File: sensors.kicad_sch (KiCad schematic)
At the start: 10 parts

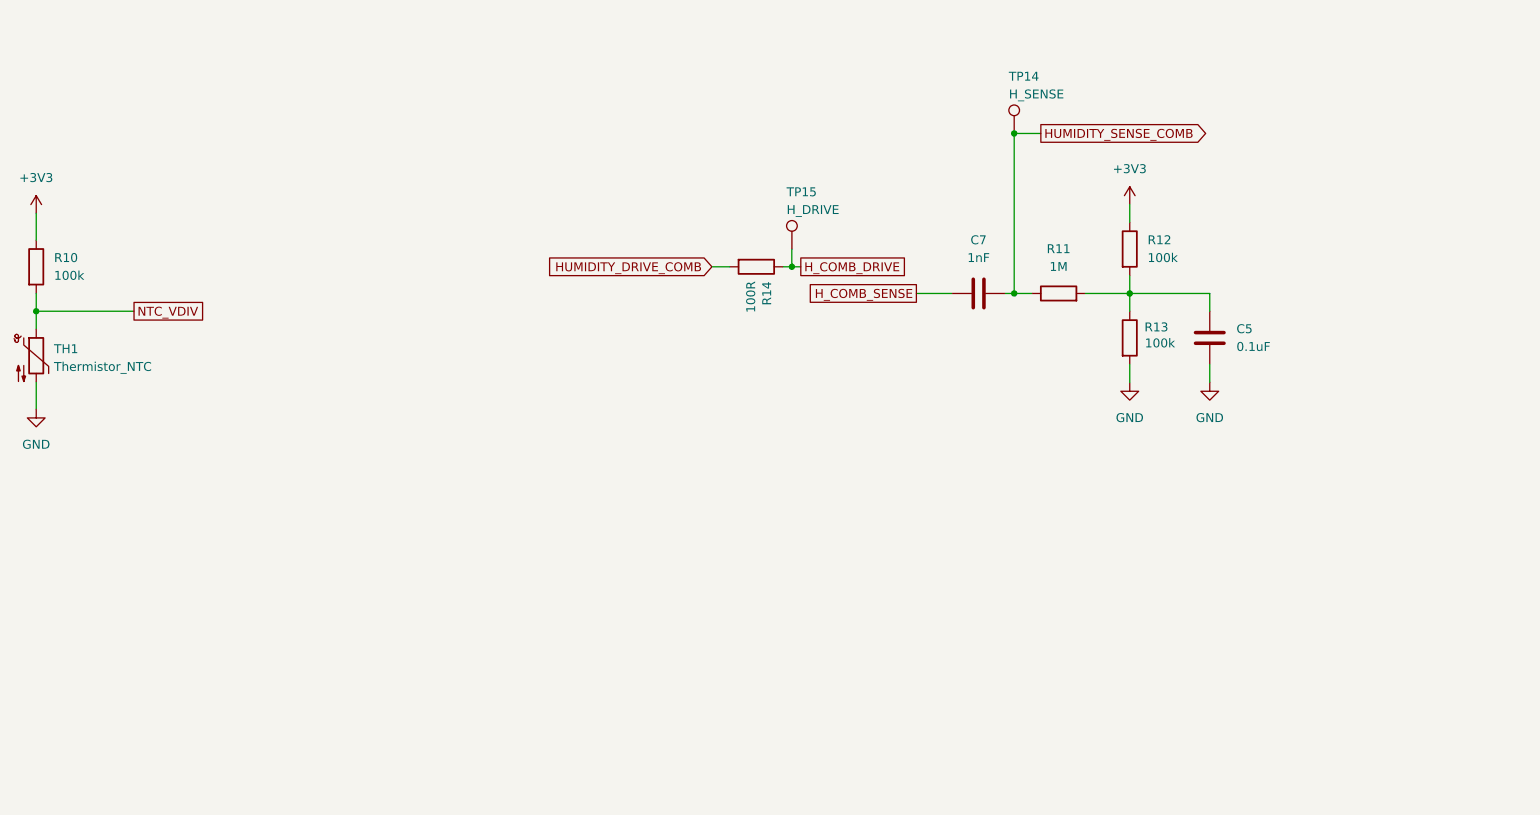
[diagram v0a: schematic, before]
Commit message: refactor hierarchical sheets to use sheet pins
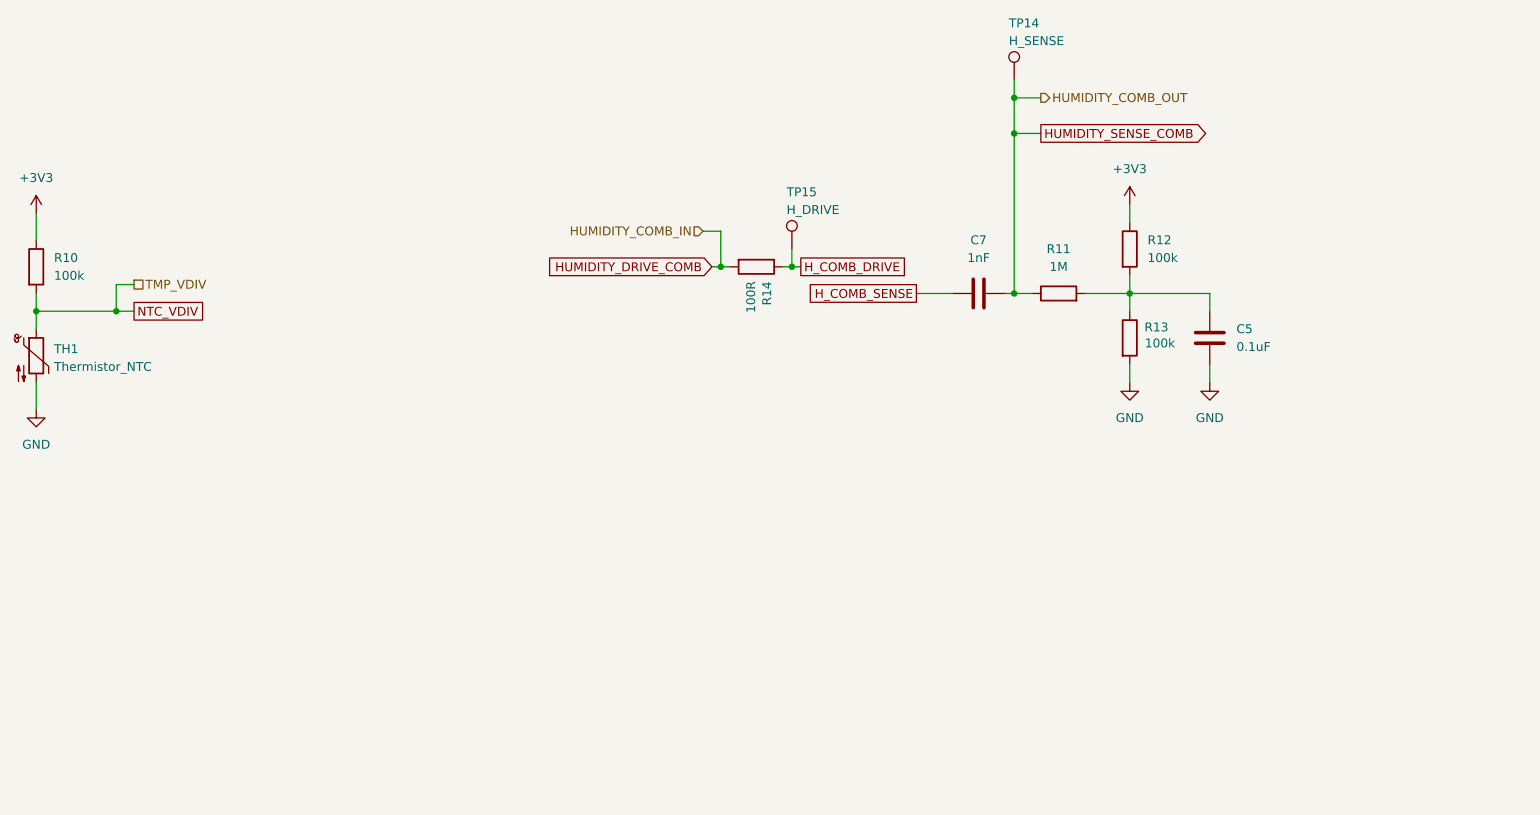
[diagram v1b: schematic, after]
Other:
- moved on the sheet: TP14
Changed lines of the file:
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@@
+	)
+	(junction
+		(at 153.67 66.04)
+		(diameter 0)
+		(color 0 0 0 0)
+	)
+	(junction
+		(at 67.31 72.39)
+		(diameter 0)
+		(color 0 0 0 0)
 	)
 	(junction
@@
 		(color 0 0 0 0)
 	)
+	(junction
+		(at 195.58 41.91)
+		(diameter 0)
+		(color 0 0 0 0)
+	)
 	(wire
 		(pts
@@
 	(wire
 		(pts
+			(xy 195.58 41.91) (xy 199.39 41.91)
+		)
+		(stroke
+			(width 0)
+			(type default)
+		)
+	)
+	(wire
+		(pts
+			(xy 67.31 72.39) (xy 69.85 72.39)
+		)
+		(stroke
+			(width 0)
+			(type default)
+		)
+	)
+	(wire
+		(pts
 			(xy 199.39 46.99) (xy 195.58 46.99)
 		)
@@
 	(wire
 		(pts
+			(xy 151.13 60.96) (xy 153.67 60.96)
+		)
+		(stroke
+			(width 0)
+			(type default)
+		)
+	)
+	(wire
+		(pts
 			(xy 195.58 46.99) (xy 195.58 69.85)
 		)
@@
 	(wire
 		(pts
+			(xy 195.58 39.37) (xy 195.58 41.91)
+		)
+		(stroke
+			(width 0)
+			(type default)
+		)
+	)
+	(wire
+		(pts
 			(xy 55.88 82.55) (xy 55.88 86.36)
 		)
@@
 	(wire
 		(pts
-			(xy 55.88 72.39) (xy 69.85 72.39)
+			(xy 153.67 66.04) (xy 152.4 66.04)
+		)
+		(stroke
+			(width 0)
+			(type default)
+		)
+	)
+	(wire
+		(pts
+			(xy 55.88 72.39) (xy 67.31 72.39)
 		)
 		(stroke
@@
 	(wire
 		(pts
+			(xy 69.85 68.58) (xy 67.31 68.58)
+		)
+		(stroke
+			(width 0)
+			(type default)
+		)
+	)
+	(wire
+		(pts
 			(xy 205.74 69.85) (xy 212.09 69.85)
 		)
@@
 	(wire
 		(pts
+			(xy 153.67 60.96) (xy 153.67 66.04)
+		)
+		(stroke
+			(width 0)
+			(type default)
+		)
+	)
+	(wire
+		(pts
 			(xy 195.58 69.85) (xy 194.31 69.85)
 		)
@@
 	(wire
 		(pts
-			(xy 154.94 66.04) (xy 152.4 66.04)
+			(xy 154.94 66.04) (xy 153.67 66.04)
 		)
 		(stroke
@@
 	(wire
 		(pts
+			(xy 195.58 41.91) (xy 195.58 46.99)
+		)
+		(stroke
+			(width 0)
+			(type default)
+		)
+	)
+	(wire
+		(pts
 			(xy 55.88 58.42) (xy 55.88 62.23)
 		)
@@
 		(pts
 			(xy 223.52 72.39) (xy 223.52 69.85)
+		)
+		(stroke
+			(width 0)
+			(type default)
+		)
+	)
+	(wire
+		(pts
+			(xy 67.31 68.58) (xy 67.31 72.39)
 		)
 		(stroke
@@
 				(hide yes)
 			)
+		)
+	)
+	(hierarchical_label "HUMIDITY_COMB_OUT"
+		(shape output)
+		(at 199.39 41.91 0)
+		(effects
+			(font
+				(size 1.27 1.27)
+			)
+			(justify left)
+		)
+	)
+	(hierarchical_label "HUMIDITY_COMB_IN"
+		(shape input)
+		(at 151.13 60.96 180)
+		(effects
+			(font
+				(size 1.27 1.27)
+			)
+			(justify right)
+		)
+	)
+	(hierarchical_label "TMP_VDIV"
+		(shape passive)
+		(at 69.85 68.58 0)
+		(effects
+			(font
+				(size 1.27 1.27)
+			)
+			(justify left)
 		)
 	)
@@
 	(symbol
 		(lib_id "Connector:TestPoint")
-		(at 195.58 46.99 0)
+		(at 195.58 39.37 0)
 		(unit 1)
 		(exclude_from_sim no)
@@
 		(dnp no)
 		(property "Reference" "TP14"
-			(at 194.818 38.862 0)
+			(at 194.818 31.242 0)
 			(effects
 				(font
@@
 		)
 		(property "Value" "H_SENSE"
-			(at 194.818 41.402 0)
+			(at 194.818 33.782 0)
 			(effects
 				(font
@@
 		)
 		(property "Footprint" "TestPoint:TestPoint_Pad_D1.5mm"
-			(at 200.66 46.99 0)
+			(at 200.66 39.37 0)
 			(effects
 				(font
@@
 		)
 		(property "Datasheet" "~"
-			(at 200.66 46.99 0)
+			(at 200.66 39.37 0)
 			(effects
 				(font
@@
 		)
 		(property "Description" "test point"
-			(at 195.58 46.99 0)
+			(at 195.58 39.37 0)
 			(effects
 				(font
@@
 		)
 		(property "AVAILABILITY" ""
-			(at 195.58 46.99 0)
+			(at 195.58 39.37 0)
 			(effects
 				(font
@@
 		)
 		(property "Availability" ""
-			(at 195.58 46.99 0)
+			(at 195.58 39.37 0)
 			(effects
 				(font
@@
 		)
 		(property "Check_prices" ""
-			(at 195.58 46.99 0)
+			(at 195.58 39.37 0)
 			(effects
 				(font
@@
 		)
 		(property "DESCRIPTION" ""
-			(at 195.58 46.99 0)
+			(at 195.58 39.37 0)
 			(effects
 				(font
@@
 		)
 		(property "Description_1" ""
-			(at 195.58 46.99 0)
+			(at 195.58 39.37 0)
 			(effects
 				(font
@@
 		)
 		(property "Est Cost AUD" ""
-			(at 195.58 46.99 0)
+			(at 195.58 39.37 0)
 			(effects
 				(font
@@
 		)
 		(property "MF" ""
-			(at 195.58 46.99 0)
+			(at 195.58 39.37 0)
 			(effects
 				(font
@@
 		)
 		(property "MP" ""
-			(at 195.58 46.99 0)
+			(at 195.58 39.37 0)
 			(effects
 				(font
@@
 		)
 		(property "PACKAGE" ""
-			(at 195.58 46.99 0)
+			(at 195.58 39.37 0)
 			(effects
 				(font
@@
 		)
 		(property "PRICE" ""
-			(at 195.58 46.99 0)
+			(at 195.58 39.37 0)
 			(effects
 				(font
@@
 		)
 		(property "Package" ""
-			(at 195.58 46.99 0)
+			(at 195.58 39.37 0)
 			(effects
 				(font
@@
 		)
 		(property "Price" ""
-			(at 195.58 46.99 0)
+			(at 195.58 39.37 0)
 			(effects
 				(font
@@
 		)
 		(property "SnapEDA_Link" ""
-			(at 195.58 46.99 0)
+			(at 195.58 39.37 0)
 			(effects
 				(font
@@
 		)
 		(property "Field6" ""
-			(at 195.58 46.99 0)
-			(effects
-				(font
+			(at 195.58 39.37 0)
+			(effects
+				(font

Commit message: WIP relayout of board
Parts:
- added C17: ~, humidity_sensors:single_layer_comb_34T, symbol humidity_sensors:humidity_comb_34T
- C5, C7: footprint Capacitor_SMD:C_0603_1608Metric -> Capacitor_SMD:C_0402_1005Metric
- R10, R11, R12, R13, R14: footprint Resistor_SMD:R_0603_1608Metric -> Resistor_SMD:R_0402_1005Metric
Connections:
- net HUMIDITY_DRIVE_COMB renamed HUMIDITY_COMB_IN
- net HUMIDITY_SENSE_COMB renamed HUMIDITY_COMB_OUT
- net H_COMB_DRIVE: no longer names the net of R14.1, TP15.1
- net H_COMB_DRIVE: now also C17.1 (in)
- net H_COMB_SENSE: no longer names the net of C7.1
- net H_COMB_SENSE: now also C17.2 (out)
- net NTC_VDIV renamed TMP_VDIV
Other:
- moved on the sheet: C5, C7, R11, R12, R13, R14, TP14, TP15

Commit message: Board V3
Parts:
- removed C5: 0.1uF, Capacitor_SMD:C_0402_1005Metric, symbol Device:C
- removed R12, R13: 100k, Resistor_SMD:R_0402_1005Metric, symbol Device:R
- added R25: 10k, Resistor_SMD:R_0402_1005Metric, symbol Device:R
- added R26: R_Photo, JCHL:SMD_3.6x2.4mm, symbol Device:R_Photo
- C17, TP14, TP15: now left out of the parts list
- C7: Est Cost 0.0029 -> (none); Est Cost (1000) (none) -> 0.0007; LCSC (none) -> https://www.lcsc.com/product-detail/C22435950.html; Manufacturer (none) -> HRE; Part No (none) -> CGA0402X7R102M500GT; Type (none) -> SMD; Vendor https://www.lcsc.com/product-detail/C6119838.html -> (none)
- R10: Est Cost 0.0007 -> (none); Est Cost (1000) (none) -> 0.0003; LCSC (none) -> https://www.lcsc.com/product-detail/C2906883.html; Manufacturer (none) -> FOJAN; Part No (none) -> FRC0402J104 TS; Type (none) -> SMD; Vendor https://www.lcsc.com/product-detail/C3017691.html -> (none)
- R11: Est Cost 0.0006 -> (none); Est Cost (1000) (none) -> 0.0004; LCSC (none) -> https://www.lcsc.com/product-detail/C2906900.html; Manufacturer (none) -> FOJAN; Part No (none) -> FRC0402J105 TS; Type (none) -> SMD; Vendor https://www.lcsc.com/product-detail/C49254192.html -> (none)
- R14: Est Cost 0.0007 -> (none); Est Cost (1000) (none) -> 0.0003; LCSC (none) -> https://www.lcsc.com/product-detail/C3017466.html; Manufacturer (none) -> VO; Part No (none) -> SCR0402J100R; Type (none) -> SMD; Vendor https://www.lcsc.com/product-detail/C2906981.html -> (none)
- TH1: Digikey (none) -> https://www.digikey.com.au/en/products/detail/ohmite/TX06F1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; Est Cost 0.05413 -> (none); Est Cost (1000) (none) -> 0.05413; Height (none) -> 0.6mm; Manufacturer (none) -> Ohmite; Part No (none) -> TX06F104F4100ER; Type (none) -> SMD; Vendor https://www.digikey.com.au/en/products/detail/ohmite/TX06F1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 -> (none)
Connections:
- net +3V3: now also R25.1
- net GND: now also R26.2
- net 1V6: now reaches R11.2
- new net LIGHT_VDIV: R25.2, R26.1
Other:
- moved on the sheet: C17, C7, R10, R11, R14, TH1, TP14, TP15
